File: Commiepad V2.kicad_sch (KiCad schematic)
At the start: 29 parts, among them J1 SSD1306 OLED, SW1 RotaryEncoder_Switch_MP, SW2 SW_Push_45deg, SW3 SW_Push_45deg, SW4 SW_Push_45deg, SW5 SW_Push_45deg, SW6 SW_Push_45deg, SW7 SW_Push_45deg, SW8 SW_Push_45deg, SW9 SW_Push_45deg, U2 XIAO-RP2040-DIP

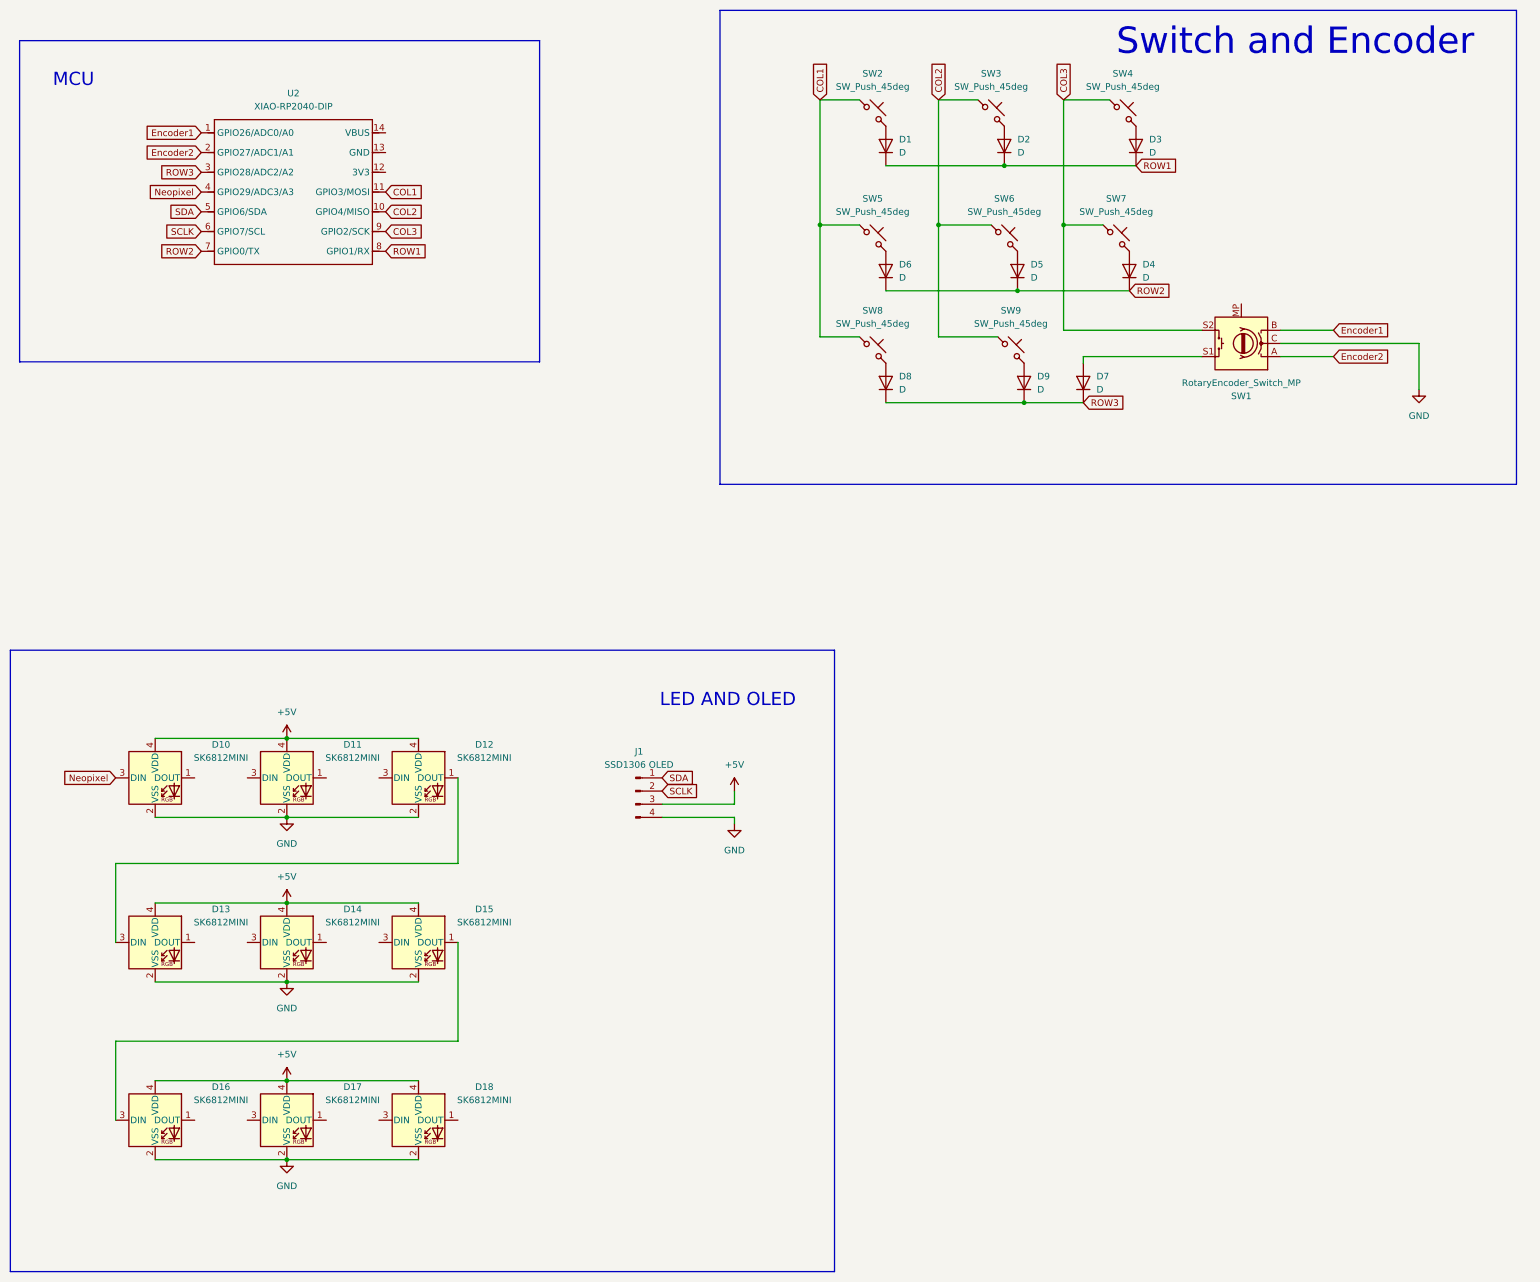
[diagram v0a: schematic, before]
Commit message: Changed the MCU to nRF52840 for wireless connectivity
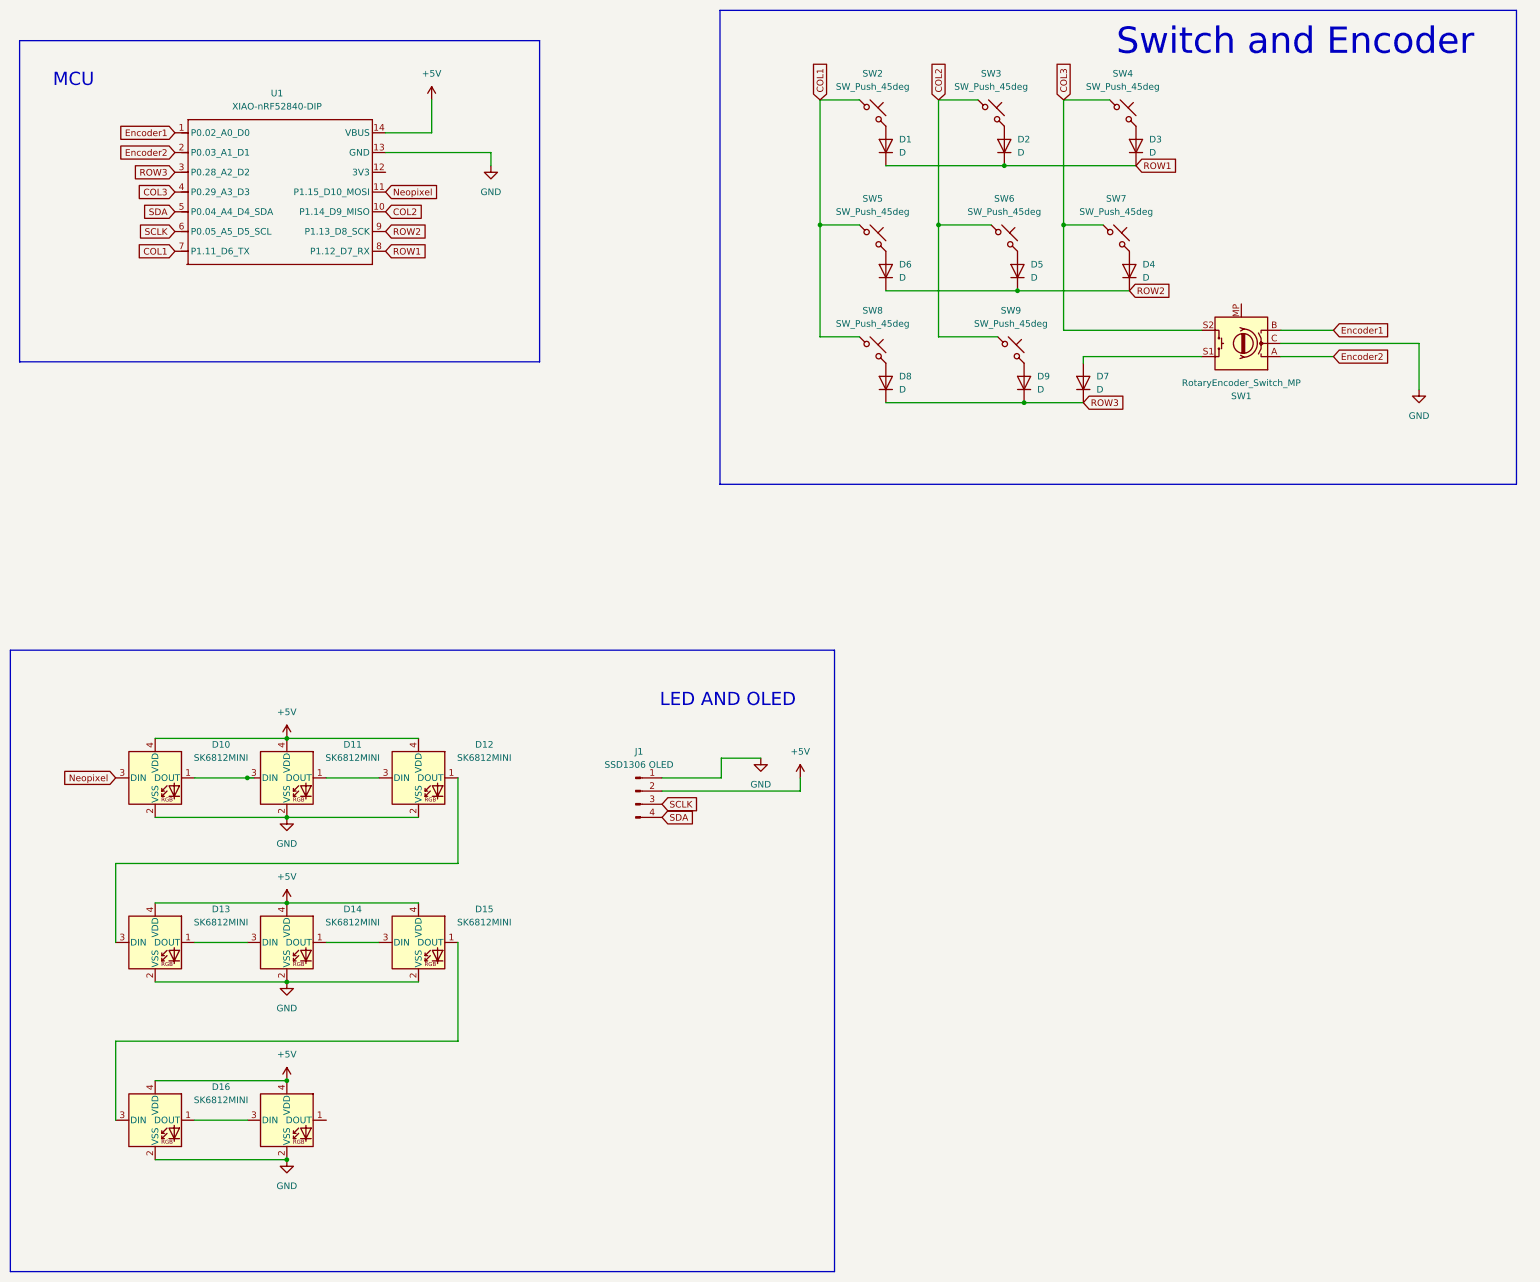
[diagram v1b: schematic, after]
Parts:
- removed D18: SK6812MINI, FSM8JH:SK6812-MINI-E, symbol LED:SK6812MINI
- removed U2: XIAO-RP2040-DIP, Seeed Studio XIAO Series Library:XIAO-RP2040-DIP, symbol OPL:XIAO-RP2040-DIP
- added U1: XIAO-nRF52840-DIP, Seeed Studio XIAO Series Library:XIAO-nRF52840-DIP, symbol Seeed_Studio_XIAO_Series:XIAO-nRF52840-DIP
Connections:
- net +5V: now also J1.2 (Pin_2), U1.14 (VBUS); no longer J1.3 (Pin_3)
- net COL1: now also U1.7 (P1.11_D6_TX)
- net COL2: now also U1.10 (P1.14_D9_MISO)
- net COL3: now also U1.4 (P0.29_A3_D3)
- net Encoder1: now also U1.1 (P0.02_A0_D0)
- net Encoder2: now also U1.2 (P0.03_A1_D1)
- net GND: now also J1.1 (Pin_1), U1.13 (GND); no longer J1.4 (Pin_4)
- net Neopixel: now also U1.11 (P1.15_D10_MOSI)
- net ROW1: now also U1.8 (P1.12_D7_RX)
- net ROW2: now also U1.9 (P1.13_D8_SCK)
- net ROW3: now also U1.3 (P0.28_A2_D2)
- net SCLK: now also J1.3 (Pin_3), U1.6 (P0.05_A5_D5_SCL); no longer J1.2 (Pin_2)
- net SDA: now also J1.4 (Pin_4), U1.5 (P0.04_A4_D4_SDA); no longer J1.1 (Pin_1)
- net at D11.1 (DOUT): now also D12.3 (DIN)
- net at D11.3 (DIN): now also D10.1 (DOUT)
- net at D17.3 (DIN): now also D16.1 (DOUT)
- net at D13.1 (DOUT): now also D14.3 (DIN)
- net at D15.3 (DIN): now also D14.1 (DOUT)

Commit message: Had to re add everything T_T
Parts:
- removed U1: XIAO-nRF52840-DIP, Seeed Studio XIAO Series Library:XIAO-nRF52840-DIP, symbol Seeed_Studio_XIAO_Series:XIAO-nRF52840-DIP
- added U1: XIAO-RP2040-DIP, Seeed Studio XIAO Series Library:XIAO-RP2040-DIP, symbol OPL:XIAO-RP2040-DIP
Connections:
- net +5V: now also U1.14 (VBUS)
- net COL1: now also U1.7 (GPIO0/TX)
- net COL2: now also U1.10 (GPIO4/MISO)
- net COL3: now also U1.4 (GPIO29/ADC3/A3)
- net Encoder1: now also U1.1 (GPIO26/ADC0/A0)
- net Encoder2: now also U1.2 (GPIO27/ADC1/A1)
- net GND: now also U1.13 (GND)
- net Neopixel: now also U1.11 (GPIO3/MOSI)
- net ROW1: now also U1.8 (GPIO1/RX)
- net ROW2: now also U1.9 (GPIO2/SCK)
- net ROW3: now also U1.3 (GPIO28/ADC2/A2)
- net SCLK: now also U1.6 (GPIO7/SCL)
- net SDA: now also U1.5 (GPIO6/SDA)
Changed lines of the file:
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@@
 	(wire
 		(pts
-			(xy 113.03 48.26) (xy 113.03 50.8)
+			(xy 107.95 48.26) (xy 107.95 50.8)
 		)
 		(stroke
@@
 	(wire
 		(pts
-			(xy 92.71 44.45) (xy 101.6 44.45)
+			(xy 87.63 44.45) (xy 96.52 44.45)
 		)
 		(stroke
@@
 	(wire
 		(pts
-			(xy 92.71 48.26) (xy 113.03 48.26)
+			(xy 87.63 48.26) (xy 107.95 48.26)
 		)
 		(stroke
@@
 	(wire
 		(pts
-			(xy 101.6 44.45) (xy 101.6 38.1)
+			(xy 96.52 44.45) (xy 96.52 38.1)
 		)
 		(stroke
@@
 	(global_label "COL2"
 		(shape input)
-		(at 92.71 59.69 0)
+		(at 87.63 59.69 0)
 		(fields_autoplaced yes)
 		(effects
@@
 		)
 		(property "Intersheetrefs" "${INTERSHEET_REFS}"
-			(at 100.5333 59.69 0)
+			(at 95.4533 59.69 0)
 			(hide yes)
 			(show_name no)
@@
 	(global_label "ROW2"
 		(shape input)
-		(at 92.71 63.5 0)
+		(at 87.63 63.5 0)
 		(fields_autoplaced yes)
 		(effects
@@
 		)
 		(property "Intersheetrefs" "${INTERSHEET_REFS}"
-			(at 100.9566 63.5 0)
+			(at 95.8766 63.5 0)
 			(hide yes)
 			(show_name no)
@@
 	(global_label "ROW1"
 		(shape input)
-		(at 92.71 67.31 0)
+		(at 87.63 67.31 0)
 		(fields_autoplaced yes)
 		(effects
@@
 		)
 		(property "Intersheetrefs" "${INTERSHEET_REFS}"
-			(at 100.9566 67.31 0)
+			(at 95.8766 67.31 0)
 			(hide yes)
 			(show_name no)
@@
 	(global_label "Neopixel"
 		(shape input)
-		(at 92.71 55.88 0)
+		(at 87.63 55.88 0)
 		(fields_autoplaced yes)
 		(effects
@@
 		)
 		(property "Intersheetrefs" "${INTERSHEET_REFS}"
-			(at 103.799 55.88 0)
+			(at 98.719 55.88 0)
 			(hide yes)
 			(show_name no)
@@
 	)
 	(symbol
-		(lib_id "Seeed_Studio_XIAO_Series:XIAO-nRF52840-DIP")
-		(at 58.42 40.64 0)
-		(unit 1)
-		(body_style 1)
-		(exclude_from_sim no)
-		(in_bom yes)
-		(on_board yes)
-		(in_pos_files yes)
-		(dnp no)
-		(fields_autoplaced yes)
-		(property "Reference" "U1"
-			(at 71.755 36.83 0)
-			(show_name no)
-			(do_not_autoplace no)
-			(effects
-				(font
-					(size 1.27 1.27)
-				)
-			)
-		)
-		(property "Value" "XIAO-nRF52840-DIP"
-			(at 71.755 39.37 0)
-			(show_name no)
-			(do_not_autoplace no)
-			(effects
-				(font
-					(size 1.27 1.27)
-				)
-			)
-		)
-		(property "Footprint" "Seeed Studio XIAO Series Library:XIAO-nRF52840-DIP"
-			(at 71.12 71.374 0)
-			(hide yes)
-			(show_name no)
-			(do_not_autoplace no)
-			(effects
-				(font
-					(size 1.27 1.27)
-				)
-			)
-		)
-		(property "Datasheet" ""
-			(at 54.61 38.1 0)
-			(hide yes)
-			(show_name no)
-			(do_not_autoplace no)
-			(effects
-				(font
-					(size 1.27 1.27)
-				)
-			)
-		)
-		(property "Description" ""
-			(at 54.61 38.1 0)
-			(hide yes)
-			(show_name no)
-			(do_not_autoplace no)
-			(effects
-				(font
-					(size 1.27 1.27)
-				)
-			)
-		)
-		(pin "1"
-		)
-		(pin "10"
-		)
-		(pin "11"
-		)
-		(pin "12"
-		)
-		(pin "14"
-		)
-		(pin "3"
-		)
-		(pin "4"
-		)
-		(pin "7"
-		)
-		(pin "2"
-		)
-		(pin "5"
-		)
-		(pin "8"
-		)
-		(pin "13"
-		)
-		(pin "9"
-		)
-		(pin "6"
-		)
-		(instances
-			(project "Commiepad V2"
-				(path "/83821413-88ad-4052-92b2-b2d32a375a4f"
-					(reference "U1")
-					(unit 1)
-				)
-			)
-		)
-	)
-	(symbol
 		(lib_id "Switch:SW_Push_45deg")
 		(at 212.09 64.77 0)
@@
 	(symbol
 		(lib_id "power:+5V")
-		(at 101.6 38.1 0)
+		(at 96.52 38.1 0)
 		(unit 1)
 		(body_style 1)
@@
 		(fields_autoplaced yes)
 		(property "Reference" "#PWR010"
-			(at 101.6 41.91 0)
+			(at 96.52 41.91 0)
 			(hide yes)
 			(show_name no)
@@
 		)
 		(property "Value" "+5V"
-			(at 101.6 33.02 0)
+			(at 96.52 33.02 0)
 			(show_name no)
 			(do_not_autoplace no)
@@
 		)
 		(property "Footprint" ""
-			(at 101.6 38.1 0)
+			(at 96.52 38.1 0)
 			(hide yes)
 			(show_name no)
@@
 		)
 		(property "Datasheet" ""
-			(at 101.6 38.1 0)
+			(at 96.52 38.1 0)
 			(hide yes)
 			(show_name no)
@@
 		)
 		(property "Description" "Power symbol creates a global label with name \"+5V\""
-			(at 101.6 38.1 0)
+			(at 96.52 38.1 0)
 			(hide yes)
 			(show_name no)
@@
 	)
 	(symbol
+		(lib_id "OPL:XIAO-RP2040-DIP")
+		(at 55.88 39.37 0)
+		(unit 1)
+		(body_style 1)
+		(exclude_from_sim no)
+		(in_bom yes)
+		(on_board yes)
+		(in_pos_files yes)
+		(dnp no)
+		(fields_autoplaced yes)
+		(property "Reference" "U1"
+			(at 69.85 36.83 0)
+			(show_name no)
+			(do_not_autoplace no)
+			(effects
+				(font
+					(size 1.27 1.27)
+				)
+			)
+		)
+		(property "Value" "XIAO-RP2040-DIP"
+			(at 69.85 39.37 0)
+			(show_name no)
+			(do_not_autoplace no)
+			(effects
+				(font
+					(size 1.27 1.27)
+				)
+			)
+		)
+		(property "Footprint" "Seeed Studio XIAO Series Library:XIAO-RP2040-DIP"
+			(at 70.358 71.628 0)
+			(hide yes)
+			(show_name no)
+			(do_not_autoplace no)
+			(effects
+				(font
+					(size 1.27 1.27)
+				)
+			)
+		)
+		(property "Datasheet" ""
+			(at 55.88 39.37 0)
+			(hide yes)
+			(show_name no)
+			(do_not_autoplace no)
+			(effects
+				(font
+					(size 1.27 1.27)
+				)
+			)
+		)
+		(property "Description" ""
+			(at 55.88 39.37 0)
+			(hide yes)
+			(show_name no)
+			(do_not_autoplace no)
+			(effects
+				(font
+					(size 1.27 1.27)
+				)
+			)
+		)
+		(pin "2"
+		)
+		(pin "1"
+		)
+		(pin "6"
+		)
+		(pin "8"
+		)
+		(pin "3"
+		)
+		(pin "7"
+		)
+		(pin "11"
+		)
+		(pin "4"
+		)
+		(pin "9"
+		)
+		(pin "5"
+		)
+		(pin "13"
+		)
+		(pin "14"
+		)
+		(pin "10"
+		)
+		(pin "12"
+		)
+		(instances
+			(project "Commiepad V2"
+				(path "/83821413-88ad-4052-92b2-b2d32a375a4f"
+					(reference "U1")
+					(unit 1)
+				)
+			)
+		)
+	)
+	(symbol
 		(lib_id "Device:D")
 		(at 189.23 46.99 90)
@@
 	(symbol
 		(lib_id "power:GND")
-		(at 113.03 50.8 0)
+		(at 107.95 50.8 0)
 		(unit 1)
 		(body_style 1)
@@
 		(fields_autoplaced yes)
 		(property "Reference" "#PWR011"
-			(at 113.03 57.15 0)
+			(at 107.95 57.15 0)
 			(hide yes)
 			(show_name no)
@@
 		)
 		(property "Value" "GND"
-			(at 113.03 55.88 0)
+			(at 107.95 55.88 0)
 			(show_name no)
 			(do_not_autoplace no)
@@
 		)
 		(property "Footprint" ""
-			(at 113.03 50.8 0)
+			(at 107.95 50.8 0)
 			(hide yes)
 			(show_name no)
@@
 		)
 		(property "Datasheet" ""
-			(at 113.03 50.8 0)
+			(at 107.95 50.8 0)
 			(hide yes)
 			(show_name no)
@@
 		)
 		(property "Description" "Power symbol creates a global label with name \"GND\" , ground"
-			(at 113.03 50.8 0)
+			(at 107.95 50.8 0)
 			(hide yes)
 			(show_name no)
